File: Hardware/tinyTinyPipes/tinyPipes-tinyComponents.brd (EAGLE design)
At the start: 59 x 59 mm, 108 parts, among them Q1 CJ2302, Q2 IRFR5305, Q3 CJ2302, Q5 S9013, Q6 S9013, Q7 S9013, U1 TD1410, U2 ICS_V54_SIM900, U3 ATMEGA168, U4 MAX4372, U5 SI4435POWER, U6 MAX4372

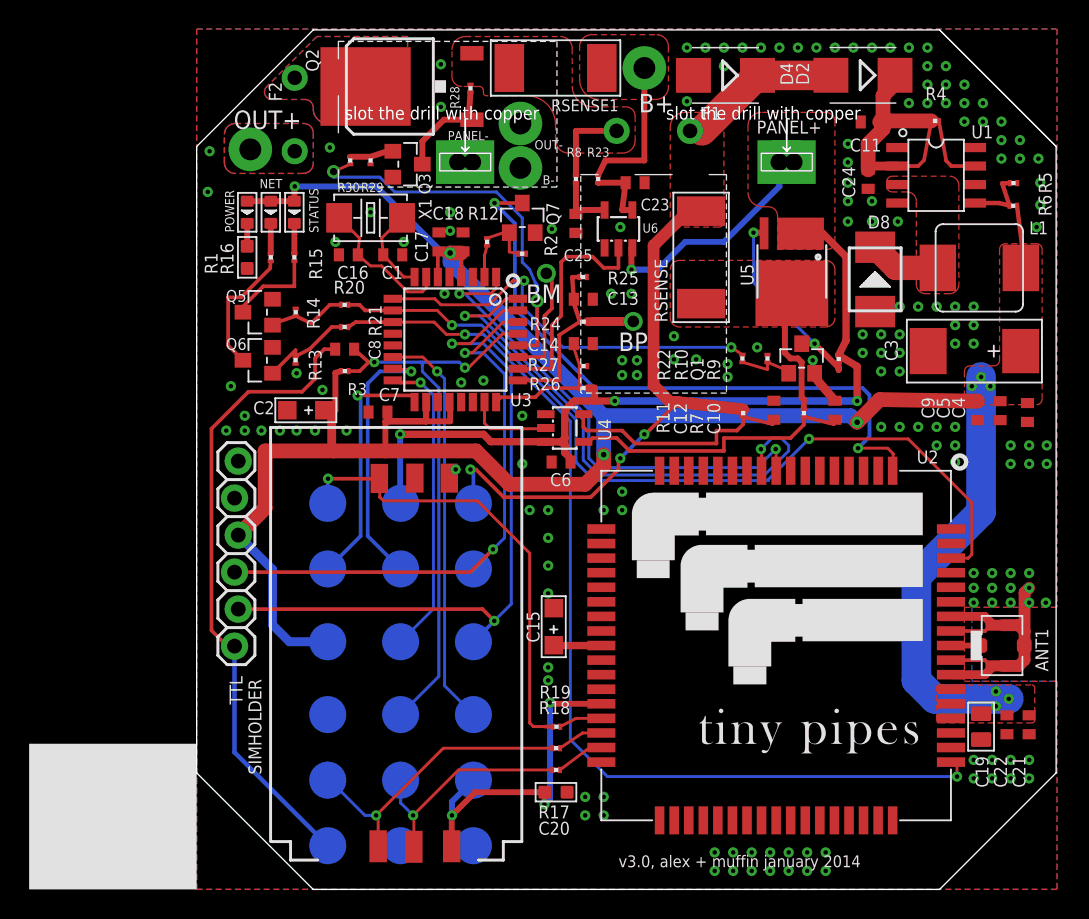
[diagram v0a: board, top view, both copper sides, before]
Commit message: netRequest is working really well -- I have the time between requests down to about 5 seconds
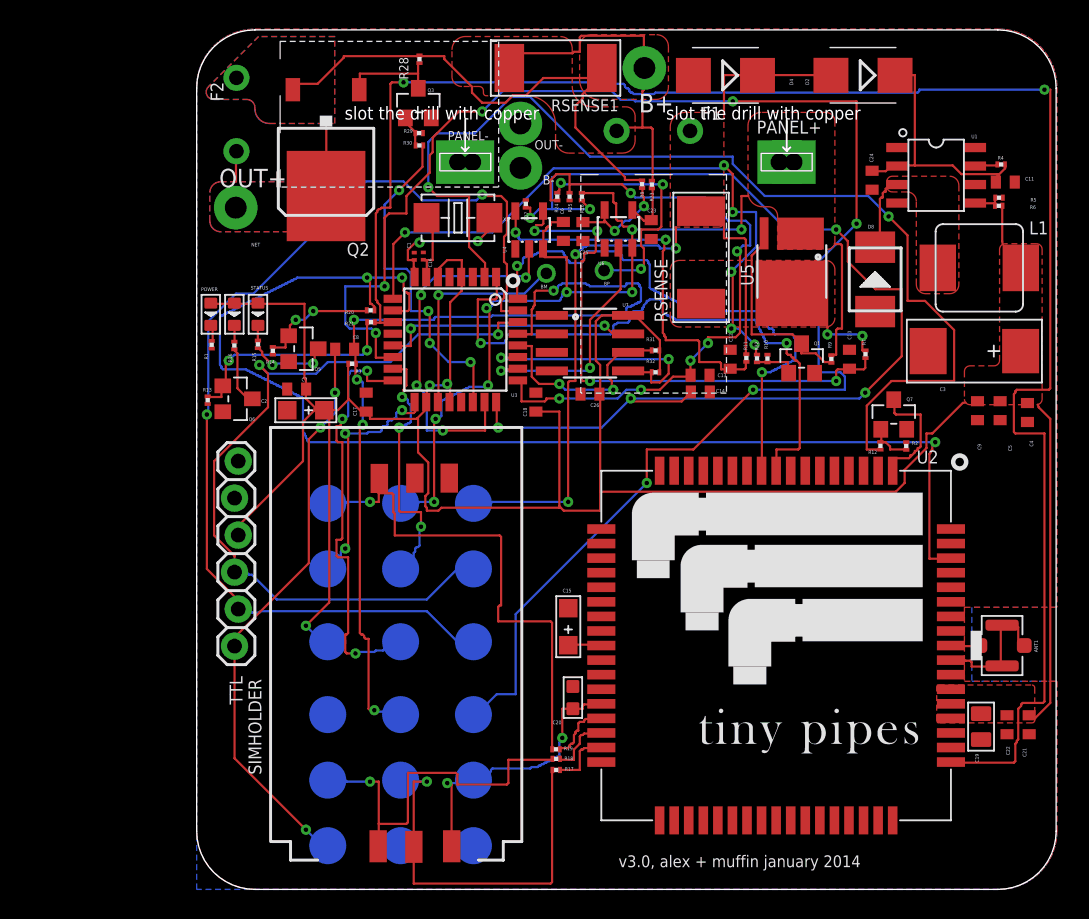
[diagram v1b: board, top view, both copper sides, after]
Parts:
- added C26: 0.1uF, rcl:C0402
- added R31, R32: 4.7k, rcl:R0201
- added U7: EEPROM-I2CSMD, SparkFun-DigitalIC:SO08
- C1, C16: device rcl:C0402 -> rcl:C0201
- R1: device Discrete:R0603 -> rcl:R0201
- moved R12 30.4 mm to (46.9, 30.4)
- moved R2 29.5 mm to (48.7, 30.4), turned to 270 degrees
- moved Q7 28.9 mm to (47.9, 32.6)
- moved C6 15.8 mm to (25.2, 45.2), turned to 90 degrees
- moved U4 13.8 mm to (22.8, 45.3), turned to 0 degrees
- moved R26 13.1 mm to (26.4, 47.6), turned to 90 degrees
- moved C17 12.1 mm to (11.6, 33.5)
- moved C18 12.1 mm to (23.3, 33.5)
- moved R27 11.8 mm to (22.6, 47.1), turned to 270 degrees
- moved C11 10.2 mm to (55.5, 48.6), turned to 180 degrees
- moved C13 9.56 mm to (34.6, 35.3), turned to 0 degrees
- moved R24 8.77 mm to (24.8, 47.6), turned to 90 degrees
- moved C14 8.69 mm to (34.6, 34.1), turned to 0 degrees
- moved NETLIGHT 7.43 mm to (2.59, 39.5)
- moved POWER 7.43 mm to (0.97, 39.5)
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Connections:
- removed net BATT: B+.1, R23.1, RSENSE1.1
- removed net N$10: F1.1, Q2.3, R28.2, R8.1, RSENSE1.2
- new net DEK: Q2.3, R28.2, R8.1, RSENSE1.1
- new net N$23: B+.1, F1.1, R23.1, RSENSE1.2
- new net SCL: R31.1, U3.28, U7.6
- new net SDA: R32.1, U3.27, U7.5
- new net WP: U3.13, U7.7
- net BATTERY_VOLTAGE: now also C13.1; no longer C13.2
- net BATT_EN: now also U3.22; no longer U3.28
- net BV-: now also U3.19; no longer U3.27
- net GND: now also C13.2, C14.2, C26.2, U7.1, U7.2, U7.3, U7.4; no longer C13.1, C14.1
- net PANEL_VOLTAGE: now also C14.1; no longer C14.2
- net VCC: now also C26.1, R31.2, R32.2, U7.8
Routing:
- net LOAD_FET: track 28.0 -> 115.3 mm, vias 1 -> 7
- net GSM_POWER: track 2.18 -> 73.3 mm, vias 0 -> 2
- net PANEL_VOLTAGE: track 9.37 -> 77.3 mm, vias 0 -> 6
- net NETLIGHT: track 69.0 -> 121.2 mm
- net DEK: track 0.00 -> 36.4 mm
- net PWRKEY: track 44.3 -> 8.26 mm, vias 2 -> 0
- net BATTERY_VOLTAGE: track 11.4 -> 45.9 mm, vias 0 -> 6
- net STATUS: track 57.6 -> 85.8 mm, vias 2 -> 3
- net TX: track 47.9 -> 72.4 mm
- net N$23: track 0.00 -> 24.0 mm
- net RST: track 40.5 -> 63.5 mm, vias 2 -> 5
- net PANEL_CURRENT: track 5.83 -> 25.7 mm, vias 0 -> 4
- net RSENSE+: track 19.9 -> 38.3 mm, vias 0 -> 4
- net WP: track 0.00 -> 17.7 mm, vias 0 -> 2
- net SDA: track 0.00 -> 17.5 mm, vias 0 -> 2
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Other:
- outline, holes or cut-outs redrawn

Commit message: pushing up tinyComponents PCB and various firmware changes
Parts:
- removed C25: 100nF, rcl:C0402
- removed F2: (no value), tinyPipes v2.6:0210
- removed OUT+, OUT-: TINYPIPES_BATTBATT, tinyPipes v2.6:TINYPIPES_BATT
- removed R29: 100k, rcl:R0201
- removed R30: 1k, rcl:R0201
- removed RSENSE1: 0.003, 1%, Discrete:R2512
- removed U6: MAX4372, tinyPipes:SOT23-5
- added D1: SS54, diode:SMB
- added Q4: BSS84, transistor-small-signal:SOT23
- added U$1: INDUCTOR, tinyPipes:10UH_5A_INDUCTOR
- C23: value 100nF -> 470uF 6.3V; device rcl:C0402 -> Discrete:AVX-D
- C4: value 10uF -> 10uF; device rcl:C0402 -> rcl:C0805
- Q2: value IRFR5305 -> CJ2302; device transistor-power:D-PAK_TO252AA -> Discrete:SOT23
- U3: value ATMEGA168 -> ATMEGA168MLF; device SparkFun:TQFP32-08 -> tinyPipes:MLF32
- X1: value (none) -> 16mhz; device Discrete:2P-SMD-5X3.2 -> tinyPipes:SMD-4_CRYSTAL
- moved C23 26.2 mm to (5.50, 40.2), turned to 180 degrees
- moved R23 13.2 mm to (20.4, 40.9)
- moved R28 12.9 mm to (19.1, 44.7), turned to 0 degrees
- moved Q3 12.3 mm to (19.2, 42.3), turned to 270 degrees
- moved R8 11.3 mm to (20.4, 43.5)
- moved C2 10.9 mm to (18.4, 33.0)
- moved Q2 9.02 mm to (16.7, 45.6), turned to 90 degrees
- moved B- 8.75 mm to (17.7, 57.0)
- moved C7 7.17 mm to (13.9, 36.0), turned to 90 degrees
- moved R21 6.22 mm to (6.97, 35.2)
- moved C4 5.91 mm to (53.5, 28.0), turned to 270 degrees
- moved Q5 5.32 mm to (11.3, 33.6)
- moved R13 5.01 mm to (5.64, 34.7), turned to 270 degrees
- moved C9 4.93 mm to (55.9, 28.5), turned to 270 degrees
- moved Q6 4.90 mm to (7.71, 33.5)
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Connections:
- removed net BATTERY_CURRENT: U3.26, U6.2
- removed net BATT_EN: R30.2, U3.22
- removed net DEK: Q2.3, R28.2, R8.1, RSENSE1.1
- removed net N$14: C25.2, R8.2, U6.5
- removed net N$18: F2.2, Q2.4
- removed net N$19: F2.1, OUT+.1
- removed net N$20: Q2.1, Q3.3, R28.1
- removed net N$21: Q3.1, R29.2, R30.1
- removed net N$23: B+.1, F1.1, R23.1, RSENSE1.2
- new net B+: B+.1, F1.1
- new net B-: B-.1, D4.A
- new net HIGH_SIDE: Q3.1, R8.2, U3.12
- new net LOW_SIDE: Q2.1, R28.2, U3.26
- new net PFET_GATE: Q3.3, Q4.1, R23.1
- new net VROUTE: C17.2, C18.2, C19.2, C2.+, C21.2, C22.2, C26.1, C3.+, C4.1, C5.1, C7.2, C9.1, L1.2, NETLIGHT.+, POWER.+, R3.2, R31.2, R32.2, R6.2, STATUS.+, TTL.4, U2.55, U2.56, U2.57, U3.18, U3.20, U3.4, U3.6, U7.8, VCC.TP
- net BATTERY: now also C23.-, R23.2, U$1.P$2
- net BV-: no longer U3.19
- net GND: now also C4.2, C5.2, C9.2, Q2.2, R28.1, R8.1; no longer B-.1, C23.2, C25.1, C4.1, C5.1, C9.1, D4.A, OUT-.1, R29.1, U6.1
- net N$17: now also C23.+, Q2.3, Q4.3; no longer C23.1, R23.2, U6.4
- net N$2: now also X1.3; no longer X1.2
- net PANEL: now also D1.A; no longer U6.3
- net VCC: now also Q4.2, U$1.P$1; no longer C17.2, C18.2, C19.2, C2.+, C21.2, C22.2, C26.1, C3.+, C4.2, C5.2, C7.2, C9.2, L1.2, NETLIGHT.+, POWER.+, R3.2, R31.2, R32.2, R6.2, STATUS.+, TTL.4, U2.55, U2.56, U2.57, U3.18, U3.20, U3.4, U3.6, U7.8, VCC.TP
- net VDD: now also D1.C
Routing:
- net VROUTE: track 0.00 -> 134.6 mm, vias 0 -> 9
- net VCC: track 171.5 -> 70.2 mm
- net LOAD_FET: track 115.3 -> 48.2 mm, vias 7 -> 3
- net NETLIGHT: track 121.2 -> 75.5 mm, vias 2 -> 6
- net BATTERY: track 54.9 -> 91.4 mm, vias 3 -> 7
- net DEK: track 36.4 -> 0.00 mm
- net PANEL_VOLTAGE: track 77.3 -> 45.8 mm, vias 6 -> 5
- net GSM_POWER: track 73.3 -> 42.9 mm
- net TX: track 72.4 -> 44.9 mm, vias 2 -> 3
- net N$23: track 24.0 -> 0.00 mm
- net BATT_EN: track 23.7 -> 0.00 mm, vias 4 -> 0
- net PANEL: track 66.1 -> 87.0 mm, vias 8 -> 2
- net BATTERY_CURRENT: track 16.6 -> 0.00 mm, vias 2 -> 0
- net GND: track 9.03 -> 24.5 mm, vias 0 -> 107
- net BV-: track 15.4 -> 0.00 mm, vias 1 -> 0
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- added copper zone on layer 1, net B+
- added copper zone on layer 1, net B-
- added copper zone on layer 1, net VROUTE
- removed copper zone on layer 1, net BATT
- removed copper zone on layer 1, net N$10
- removed copper zone on layer 1, net N$18
- removed copper zone on layer 16, net N$18
- removed copper zone on layer 1, net N$19
- removed copper zone on layer 16, net N$19
- removed copper zone on layer 1, net VCC
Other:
- board size 59 x 59 mm -> 59.1 x 59 mm
- board text added: "january 18, 2014"
- board text removed: "v3.0, alex + muffin january 2014"
